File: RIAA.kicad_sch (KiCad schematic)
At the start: 61 parts, among them K1 G6K-2, P10 From Keyboard, P8 From main PCB, P9 From Wire, Q1 BCV49, U5 OPA2134, U6 OPA2134, U7 LM317_TO-220

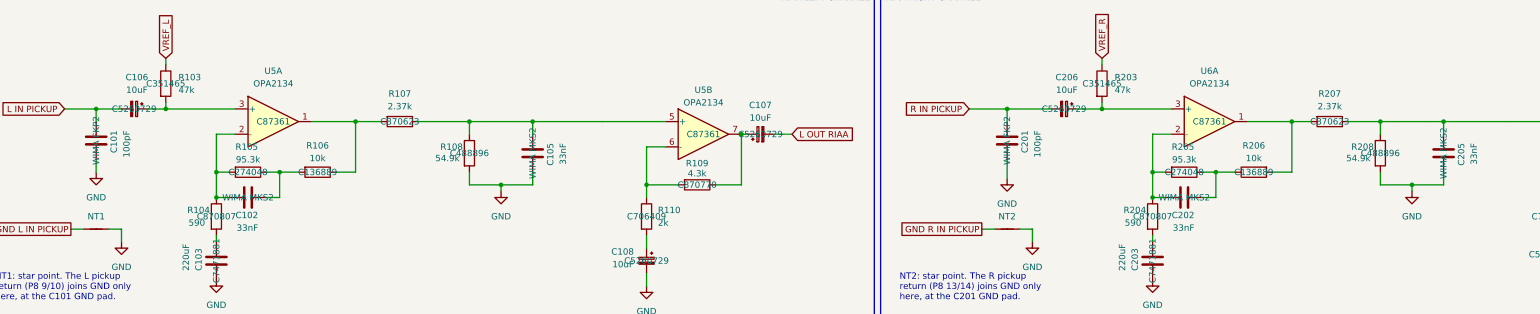
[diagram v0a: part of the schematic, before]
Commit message: Add manufacturer part numbers and PCBWay turnkey BOM
Every part now carries Manufacturer and MPN fields in the schematic and
on the board, next to the existing LCSC numbers. The film capacitors get
full WIMA part numbers instead of series names and Mouser links.

make_bom.py additionally writes RIAA-bom-pcbway.csv (all parts by MPN,
with LCSC as distributor PN) and RIAA-cpl-pcbway.csv (SMD parts only);
the JLCPCB files are unchanged. CI attaches both to releases.

The board's zones and teardrops are rebuilt after the output meanders
were removed, which also clears a stale zone clearance violation on
R OUT. README render, docs and changelog updated.

Co-Authored-By: Claude Opus 5.5 <noreply@anthropic.com>
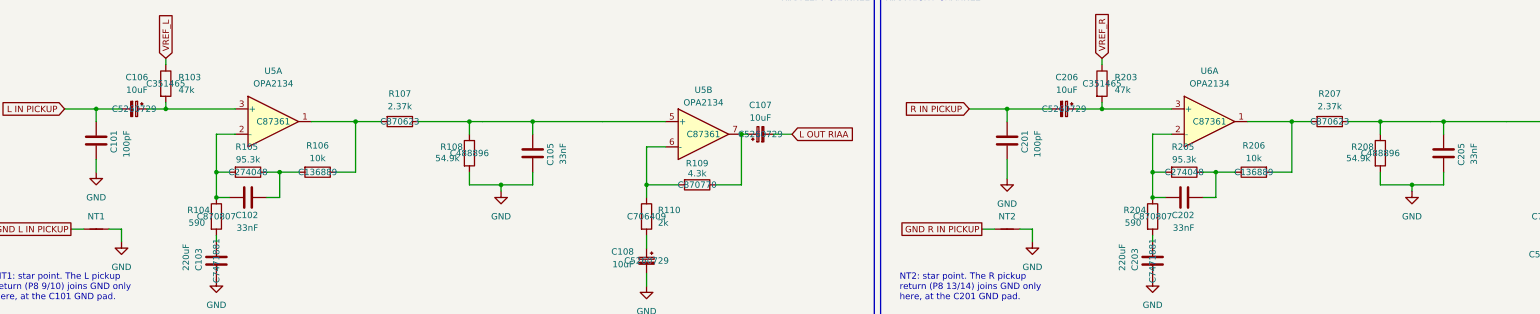
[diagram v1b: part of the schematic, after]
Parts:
- C1: MPN (none) -> VZH471M1VTR-1013L; Manufacturer (none) -> Lelon
- C101, C201: MPN (none) -> FKP2D001001D00JSSD; Manufacturer (none) -> WIMA; PN WIMA FKP2 -> (none)
- C102, C105, C202, C205: MPN (none) -> MKS2C023301A00JSSD; Manufacturer (none) -> WIMA; PN WIMA MKS2 -> (none)
- C103, C203: MPN (none) -> 189RV0019; Manufacturer (none) -> KNSCHA
- C106, C107, C108, C206, C207, C208, C34, C35: MPN (none) -> FZ1V100M0506; Manufacturer (none) -> JARSON
- C27, C28, C29: MPN (none) -> CL31B104KBCNNNC; Manufacturer (none) -> Samsung Electro-Mechanics
- C30: MPN (none) -> CL31A106KBHNNNE; Manufacturer (none) -> Samsung Electro-Mechanics
- C33: MPN (none) -> HGC1206R5107M100NSPJ; Manufacturer (none) -> Chinocera
- D5, D7, D8: MPN (none) -> 1N4004G; Manufacturer (none) -> Shikues
- D6: MPN (none) -> 1N4002G; Manufacturer (none) -> Shikues
- K1: MPN (none) -> G6K-2F-Y-TR DC24; Manufacturer (none) -> OMRON
- P10, P8: MPN (none) -> PM254-2-09-W-8.5; Manufacturer (none) -> HCTL
- P9: MPN (none) -> 2.54-1*6P; Manufacturer (none) -> BOOMELE
- Q1: MPN (none) -> BCV49TA; Manufacturer (none) -> Diodes Incorporated
- R103, R203: MPN (none) -> PTFR1206B47K0P9; Manufacturer (none) -> RESI
- R104, R204: MPN (none) -> RT1206BRD07590RL; Manufacturer (none) -> YAGEO
- R105, R205: MPN (none) -> RC1206FR-0795K3L; Manufacturer (none) -> YAGEO
- R106, R206: MPN (none) -> RT1206BRD0710KL; Manufacturer (none) -> YAGEO
- R107, R207: MPN (none) -> RT1206BRD072K37L; Manufacturer (none) -> YAGEO
- R108, R208: MPN (none) -> RC1206FR-0754K9L; Manufacturer (none) -> YAGEO
- R109, R209: MPN (none) -> RT1206BRD074K3L; Manufacturer (none) -> YAGEO
- R110, R210: MPN (none) -> RT1206BRD072KL; Manufacturer (none) -> YAGEO
- R19: MPN (none) -> 1206W4F4701T5E; Manufacturer (none) -> UNI-ROYAL
- R20: MPN (none) -> RT1206BRD07300RL; Manufacturer (none) -> YAGEO
- R21: MPN (none) -> 1206W4F1001T5E; Manufacturer (none) -> UNI-ROYAL
- R22, R23, R24, R25, R26: MPN (none) -> 1206W4F1003T5E; Manufacturer (none) -> UNI-ROYAL
- RV1: MPN (none) -> 3314G-1-105E; Manufacturer (none) -> Bourns
- U5, U6: MPN (none) -> OPA2134UA/2K5; Manufacturer (none) -> Texas Instruments
- U7: MPN (none) -> LM317D2TR4G; Manufacturer (none) -> onsemi

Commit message: Ceramic capacitors, 38 dB gain, output resistors and 4004 checks
- C1, C34/C35 and C107/C207 are now 1206 ceramics (C34/C35 22 uF to
  allow for DC-bias loss); the six remaining electrolytics are where a
  ceramic would be microphonic or add distortion (see design notes).
- R109/R209 4.3k -> 7.5k (RESI PTFR1206B7K50P9, C351451): gain about
  38 dB, to suit B&O's low-output MMC cartridges.
- New R113/R213 (100 R, C17901) between each op-amp output and its
  output capacitor, outside the feedback loop.
- P9 pins 2/4 are no-connects, matching the original P9 pin layout, so
  a 4004 harness no longer shorts the Beomaster 2400 remote lines; a
  ground via keeps K1's mute contact on the plane.
- Checked against the BeoGram 4004 service manual: P10 power pins match
  the 4004 module (8005022); its remote circuit is not supported.
- U7 value "LM317", 0.15 mm stroke on the section labels, datasheet
  fields synced, teardrops and zones rebuilt; ERC/DRC clean.
- README, design notes, changelog, render and response chart updated.

Co-Authored-By: Claude Opus 5.5 <noreply@anthropic.com>
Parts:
- added R113, R213: 100, Resistor_SMD:R_1206_3216Metric_Pad1.30x1.75mm_HandSolder, symbol Device:R
- C1: value 470uF -> 10uF; footprint Capacitor_SMD:CP_Elec_10x10.5 -> Capacitor_SMD:C_1206_3216Metric_Pad1.33x1.80mm_HandSolder; symbol Device:C_Polarized_Small -> Device:C_Small; LCSC PN C134524 -> C13585; MPN VZH471M1VTR-1013L -> CL31A106KBHNNNE; Manufacturer Lelon -> Samsung Electro-Mechanics
- C107, C207: footprint Capacitor_SMD:CP_Elec_5x5.4 -> Capacitor_SMD:C_1206_3216Metric_Pad1.33x1.80mm_HandSolder; symbol Device:C_Polarized_Small -> Device:C_Small; LCSC PN C5260729 -> C13585; MPN FZ1V100M0506 -> CL31A106KBHNNNE; Manufacturer JARSON -> Samsung Electro-Mechanics
- C29, C30, C33: symbol Device:C_Polarized_Small -> Device:C_Small
- C34, C35: value 10uF -> 22uF; footprint Capacitor_SMD:CP_Elec_5x5.4 -> Capacitor_SMD:C_1206_3216Metric_Pad1.33x1.80mm_HandSolder; symbol Device:C_Polarized_Small -> Device:C_Small; LCSC PN C5260729 -> C12891; MPN FZ1V100M0506 -> CL31A226KAHNNNE; Manufacturer JARSON -> Samsung Electro-Mechanics
- R109, R209: value 4.3k -> 7.5k; LCSC PN C870770 -> C351451; MPN RT1206BRD074K3L -> PTFR1206B7K50P9; Manufacturer YAGEO -> RESI
- U7: value LM317_TO-220 -> LM317
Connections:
- net GND: no longer P9.2 (Pin_2), P9.4 (Pin_4)
- net at R209.1, U6.7: now also R213.2; no longer C207.1
- net at R109.1, U5.7: now also R113.2; no longer C107.1
- new net: C207.1, R213.1
- new net: C107.1, R113.1
- no-connect marks 15 -> 17

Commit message: Schematic tidy-up: ERC without warnings, relay part named
- D5-D8 use the plain diode symbol (were drawn as Zeners; same pins).
- Duplicate net names removed: GND MB and GND CHASSIS labels are now
  GND, L/R OUT RIAA are now L/R OUT. Connectivity is unchanged
  (netlist compared before and after).
- RV1's embedded symbol matches the library.
- K1 value reads G6K-2F-Y DC24, the 24 V part already on the BOM.
- POWER silkscreen outline and label moved 0.7 mm left, off R24's pad.
- Design notes: relay contacts described correctly (commons 3/6 on GND,
  normally-closed 2/7 on the outputs); README names the 24 V relay.

ERC: 0 errors, 0 warnings. DRC: 0 errors, 0 unconnected, 0 parity
issues; the only notes are P8/P9/P10 having teardrops on their pads.

Co-Authored-By: Claude Opus 5.5 <noreply@anthropic.com>
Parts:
- D5, D6, D7, D8: symbol Device:D_Zener -> Device:D
- K1: value G6K-2 -> G6K-2F-Y DC24
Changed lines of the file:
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@@
 		)
 	)
-	(global_label "GND MB"
+	(global_label "GND"
 		(shape input)
 		(at 213.36 151.13 270)
@@
 		)
 	)
-	(global_label "R OUT RIAA"
+	(global_label "R OUT"
 		(shape input)
 		(at 266.7 173.99 90)
@@
 		)
 	)
-	(global_label "R OUT RIAA"
+	(global_label "R OUT"
 		(shape input)
 		(at 414.02 85.09 0)
@@
 		)
 	)
-	(global_label "GND MB"
+	(global_label "GND"
 		(shape input)
 		(at 346.71 190.5 90)
@@
 		)
 	)
-	(global_label "L OUT RIAA"
+	(global_label "L OUT"
 		(shape input)
 		(at 276.86 173.99 90)
@@
 		)
 	)
-	(global_label "L OUT RIAA"
+	(global_label "L OUT"
 		(shape input)
 		(at 227.33 85.09 0)
@@
 		)
 	)
-	(global_label "GND MB"
+	(global_label "GND"
 		(shape input)
 		(at 58.42 180.34 180)
@@
 		)
 	)
-	(global_label "GND CHASSIS"
+	(global_label "GND"
 		(shape input)
 		(at 243.84 128.27 0)
@@
 		)
 	)
-	(global_label "GND CHASSIS"
+	(global_label "GND"
 		(shape input)
 		(at 403.86 149.86 90)
@@
 			)
 		)
-		(property "Value" "G6K-2"
+		(property "Value" "G6K-2F-Y DC24"
 			(at 286.258 186.69 0)
 			(effects
@@
 	)
 	(symbol
-		(lib_id "Device:D_Zener")
+		(lib_id "Device:D")
 		(at 243.84 149.86 0)
 		(mirror x)
@@
 			)
 		)
-		(property "Description" "Zener diode"
+		(property "Description" "Diode"
 			(at 243.84 149.86 0)
 			(effects
@@
 	)
 	(symbol
-		(lib_id "Device:D_Zener")
+		(lib_id "Device:D")
 		(at 104.14 165.1 90)
 		(mirror x)
@@
 			)
 		)
-		(property "Description" "Zener diode"
+		(property "Description" "Diode"
 			(at 104.14 165.1 0)
 			(effects
@@
 	)
 	(symbol
-		(lib_id "Device:D_Zener")
+		(lib_id "Device:D")
 		(at 78.74 148.59 0)
 		(unit 1)
@@
 			)
 		)
-		(property "Description" "Zener diode"
+		(property "Description" "Diode"
 			(at 78.74 148.59 0)
 			(effects
@@
 	)
 	(symbol
-		(lib_id "Device:D_Zener")
+		(lib_id "Device:D")
 		(at 220.98 176.53 90)
 		(unit 1)
@@
 			)
 		)
-		(property "Description" "Zener diode"
+		(property "Description" "Diode"
 			(at 220.98 176.53 0)
 			(effects
